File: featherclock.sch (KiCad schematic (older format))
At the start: 49 parts, among them J1 feather long, J2 feather short, J3 Conn_01x04, J4 USB_C_Receptacle_USB2.0, Q1 MMBT3904, Q2 MMBT3904, SW1 SW_Push, U1 ESP8285, U2 DS3231MZ, U3 74AHCT1G125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

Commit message: Updated most 0603 packages to 0402
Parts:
- C1, C2: footprint Capacitor_SMD:C_0603_1608Metric -> Capacitor_SMD:C_0402_1005Metric; LCSC C15849 -> C52923
- C10, C11, C12, C13, C4, C5, C9: footprint Capacitor_SMD:C_0603_1608Metric -> Capacitor_SMD:C_0402_1005Metric; LCSC C14663 -> C1525
- L1: footprint Inductors_SMD:L_0603 -> Inductors_SMD:L_0402; LCSC C1030 -> C13595
- R1, R12, R3, R4, R5, R6, R8, R9: footprint Resistor_SMD:R_0603_1608Metric -> Resistor_SMD:R_0402_1005Metric; LCSC C23162 -> C25900
- R10, R11: footprint Resistor_SMD:R_0603_1608Metric -> Resistor_SMD:R_0402_1005Metric; LCSC C25804 -> C25744
- R13, R14: footprint Resistor_SMD:R_0603_1608Metric -> Resistor_SMD:R_0402_1005Metric; LCSC C23186 -> C25905
- R2: footprint Resistor_SMD:R_0603_1608Metric -> Resistor_SMD:R_0402_1005Metric; LCSC C22790 -> C25752
- R7: footprint Resistor_SMD:R_0603_1608Metric -> Resistor_SMD:R_0402_1005Metric; LCSC C22775 -> C25076
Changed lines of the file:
@@
 F 0 "R2" H 3320 3896 50  0000 L CNN
 F 1 "12K" H 3320 3805 50  0000 L CNN
-F 2 "Resistor_SMD:R_0603_1608Metric" V 3180 3850 50  0001 C CNN
+F 2 "Resistor_SMD:R_0402_1005Metric" V 3180 3850 50  0001 C CNN
 F 3 "~" H 3250 3850 50  0001 C CNN
-F 4 "C22790" H 3250 3850 50  0001 C CNN "LCSC"
+F 4 "C25752" H 3250 3850 50  0001 C CNN "LCSC"
 	1    3250 3850
 	1    0    0    -1
@@
 F 0 "R1" H 4170 3296 50  0000 L CNN
 F 1 "4.7K" H 4170 3205 50  0000 L CNN
-F 2 "Resistor_SMD:R_0603_1608Metric" V 4030 3250 50  0001 C CNN
+F 2 "Resistor_SMD:R_0402_1005Metric" V 4030 3250 50  0001 C CNN
 F 3 "~" H 4100 3250 50  0001 C CNN
-F 4 "C23162" H 4100 3250 50  0001 C CNN "LCSC"
+F 4 "C25900" H 4100 3250 50  0001 C CNN "LCSC"
 	1    4100 3250
 	1    0    0    -1
@@
 F 0 "R4" H 2820 4446 50  0000 L CNN
 F 1 "4.7K" H 2820 4355 50  0000 L CNN
-F 2 "Resistor_SMD:R_0603_1608Metric" V 2680 4400 50  0001 C CNN
+F 2 "Resistor_SMD:R_0402_1005Metric" V 2680 4400 50  0001 C CNN
 F 3 "~" H 2750 4400 50  0001 C CNN
-F 4 "C23162" H 2750 4400 50  0001 C CNN "LCSC"
+F 4 "C25900" H 2750 4400 50  0001 C CNN "LCSC"
 	1    2750 4400
 	1    0    0    -1
@@
 F 0 "C1" H 8265 3846 50  0000 L CNN
 F 1 "1u" H 8265 3755 50  0000 L CNN
-F 2 "Capacitor_SMD:C_0603_1608Metric" H 8188 3650 50  0001 C CNN
+F 2 "Capacitor_SMD:C_0402_1005Metric" H 8188 3650 50  0001 C CNN
 F 3 "~" H 8150 3800 50  0001 C CNN
-F 4 "C15849" H 8150 3800 50  0001 C CNN "LCSC"
+F 4 "C52923" H 8150 3800 50  0001 C CNN "LCSC"
 	1    8150 3800
 	1    0    0    -1
@@
 F 0 "C2" H 8765 3846 50  0000 L CNN
 F 1 "1u" H 8765 3755 50  0000 L CNN
-F 2 "Capacitor_SMD:C_0603_1608Metric" H 8688 3650 50  0001 C CNN
+F 2 "Capacitor_SMD:C_0402_1005Metric" H 8688 3650 50  0001 C CNN
 F 3 "~" H 8650 3800 50  0001 C CNN
-F 4 "C15849" H 8650 3800 50  0001 C CNN "LCSC"
+F 4 "C52923" H 8650 3800 50  0001 C CNN "LCSC"
 	1    8650 3800
 	1    0    0    -1
@@
 F 0 "C4" H 9765 3846 50  0000 L CNN
 F 1 "100n" H 9765 3755 50  0000 L CNN
-F 2 "Capacitor_SMD:C_0603_1608Metric" H 9688 3650 50  0001 C CNN
+F 2 "Capacitor_SMD:C_0402_1005Metric" H 9688 3650 50  0001 C CNN
 F 3 "~" H 9650 3800 50  0001 C CNN
-F 4 "C14663" H 9650 3800 50  0001 C CNN "LCSC"
+F 4 "C1525" H 9650 3800 50  0001 C CNN "LCSC"
 	1    9650 3800
 	1    0    0    -1
@@
 F 0 "R3" H 2570 4446 50  0000 L CNN
 F 1 "4.7K" H 2570 4355 50  0000 L CNN
-F 2 "Resistor_SMD:R_0603_1608Metric" V 2430 4400 50  0001 C CNN
+F 2 "Resistor_SMD:R_0402_1005Metric" V 2430 4400 50  0001 C CNN
 F 3 "~" H 2500 4400 50  0001 C CNN
-F 4 "C23162" H 2500 4400 50  0001 C CNN "LCSC"
+F 4 "C25900" H 2500 4400 50  0001 C CNN "LCSC"
 	1    2500 4400
 	1    0    0    -1
@@
 F 0 "C5" H 6115 3296 50  0000 L CNN
 F 1 "100n" H 6115 3205 50  0000 L CNN
-F 2 "Capacitor_SMD:C_0603_1608Metric" H 6038 3100 50  0001 C CNN
+F 2 "Capacitor_SMD:C_0402_1005Metric" H 6038 3100 50  0001 C CNN
 F 3 "~" H 6000 3250 50  0001 C CNN
-F 4 "C14663" H 6000 3250 50  0001 C CNN "LCSC"
+F 4 "C1525" H 6000 3250 50  0001 C CNN "LCSC"
 	1    6000 3250
 	1    0    0    -1
@@
 F 0 "L1" V 6440 3000 50  0000 C CNN
 F 1 "4.7n" V 6349 3000 50  0000 C CNN
-F 2 "Inductors_SMD:L_0603" H 6250 3000 50  0001 C CNN
+F 2 "Inductors_SMD:L_0402" H 6250 3000 50  0001 C CNN
 F 3 "~" H 6250 3000 50  0001 C CNN
-F 4 "C1030" V 6250 3000 50  0001 C CNN "LCSC"
+F 4 "C13595" V 6250 3000 50  0001 C CNN "LCSC"
 	1    6250 3000
 	0    -1   -1   0
@@
 F 0 "R7" V 5543 6500 50  0000 C CNN
 F 1 "100" V 5634 6500 50  0000 C CNN
-F 2 "Resistor_SMD:R_0603_1608Metric" V 5680 6500 50  0001 C CNN
+F 2 "Resistor_SMD:R_0402_1005Metric" V 5680 6500 50  0001 C CNN
 F 3 "~" H 5750 6500 50  0001 C CNN
-F 4 "C22775" H 5750 6500 50  0001 C CNN "LCSC"
+F 4 "C25076" H 5750 6500 50  0001 C CNN "LCSC"
 	1    5750 6500
 	0    1    1    0
@@
 F 0 "R5" H 2620 2246 50  0000 L CNN
 F 1 "4.7K" H 2620 2155 50  0000 L CNN
-F 2 "Resistor_SMD:R_0603_1608Metric" V 2480 2200 50  0001 C CNN
+F 2 "Resistor_SMD:R_0402_1005Metric" V 2480 2200 50  0001 C CNN
 F 3 "~" H 2550 2200 50  0001 C CNN
-F 4 "C23162" H 2550 2200 50  0001 C CNN "LCSC"
+F 4 "C25900" H 2550 2200 50  0001 C CNN "LCSC"
 	1    2550 2200
 	0    -1   -1   0
@@
 F 0 "R9" H 3570 5296 50  0000 L CNN
 F 1 "4.7K" H 3570 5205 50  0000 L CNN
-F 2 "Resistor_SMD:R_0603_1608Metric" V 3430 5250 50  0001 C CNN
+F 2 "Resistor_SMD:R_0402_1005Metric" V 3430 5250 50  0001 C CNN
 F 3 "~" H 3500 5250 50  0001 C CNN
-F 4 "C23162" H 3500 5250 50  0001 C CNN "LCSC"
+F 4 "C25900" H 3500 5250 50  0001 C CNN "LCSC"
 	1    3500 5250
 	-1   0    0    1
@@
 F 0 "C11" H 5615 6196 50  0000 L CNN
 F 1 "100n" H 5615 6105 50  0000 L CNN
-F 2 "Capacitor_SMD:C_0603_1608Metric" H 5538 6000 50  0001 C CNN
+F 2 "Capacitor_SMD:C_0402_1005Metric" H 5538 6000 50  0001 C CNN
 F 3 "~" H 5500 6150 50  0001 C CNN
-F 4 "C14663" H 5500 6150 50  0001 C CNN "LCSC"
+F 4 "C1525" H 5500 6150 50  0001 C CNN "LCSC"
 	1    5500 6150
 	1    0    0    -1
@@
 F 0 "R11" V 1293 7300 50  0000 C CNN
 F 1 "10K" V 1384 7300 50  0000 C CNN
-F 2 "Resistor_SMD:R_0603_1608Metric" V 1430 7300 50  0001 C CNN
+F 2 "Resistor_SMD:R_0402_1005Metric" V 1430 7300 50  0001 C CNN
 F 3 "~" H 1500 7300 50  0001 C CNN
-F 4 "C25804" H 1500 7300 50  0001 C CNN "LCSC"
+F 4 "C25744" H 1500 7300 50  0001 C CNN "LCSC"
 	1    1500 7300
 	0    1    1    0
@@
 F 0 "R10" V 1293 6700 50  0000 C CNN
 F 1 "10K" V 1384 6700 50  0000 C CNN
-F 2 "Resistor_SMD:R_0603_1608Metric" V 1430 6700 50  0001 C CNN
+F 2 "Resistor_SMD:R_0402_1005Metric" V 1430 6700 50  0001 C CNN
 F 3 "~" H 1500 6700 50  0001 C CNN
-F 4 "C25804" H 1500 6700 50  0001 C CNN "LCSC"
+F 4 "C25744" H 1500 6700 50  0001 C CNN "LCSC"
 	1    1500 6700
 	0    1    1    0
@@
 F 0 "R6" H 3870 3296 50  0000 L CNN
 F 1 "4.7K" H 3870 3205 50  0000 L CNN
-F 2 "Resistor_SMD:R_0603_1608Metric" V 3730 3250 50  0001 C CNN
+F 2 "Resistor_SMD:R_0402_1005Metric" V 3730 3250 50  0001 C CNN
 F 3 "~" H 3800 3250 50  0001 C CNN
-F 4 "C23162" H 3800 3250 50  0001 C CNN "LCSC"
+F 4 "C25900" H 3800 3250 50  0001 C CNN "LCSC"
 	1    3800 3250
 	1    0    0    -1
@@
 F 0 "R12" H 3920 9246 50  0000 L CNN
 F 1 "4.7K" H 3920 9155 50  0000 L CNN
-F 2 "Resistor_SMD:R_0603_1608Metric" V 3780 9200 50  0001 C CNN
+F 2 "Resistor_SMD:R_0402_1005Metric" V 3780 9200 50  0001 C CNN
 F 3 "~" H 3850 9200 50  0001 C CNN
-F 4 "C23162" H 3850 9200 50  0001 C CNN "LCSC"
+F 4 "C25900" H 3850 9200 50  0001 C CNN "LCSC"
 	1    3850 9200
 	0    -1   -1   0
@@
 F 0 "C13" H 4465 9546 50  0000 L CNN
 F 1 "100n" H 4465 9455 50  0000 L CNN
-F 2 "Capacitor_SMD:C_0603_1608Metric" H 4388 9350 50  0001 C CNN
+F 2 "Capacitor_SMD:C_0402_1005Metric" H 4388 9350 50  0001 C CNN
 F 3 "~" H 4350 9500 50  0001 C CNN
-F 4 "C14663" H 4350 9500 50  0001 C CNN "LCSC"
+F 4 "C1525" H 4350 9500 50  0001 C CNN "LCSC"
 	1    4350 9500
 	1    0    0    -1
@@
 F 0 "C12" H 2665 9196 50  0000 L CNN
 F 1 "100n" H 2665 9105 50  0000 L CNN
-F 2 "Capacitor_SMD:C_0603_1608Metric" H 2588 9000 50  0001 C CNN
+F 2 "Capacitor_SMD:C_0402_1005Metric" H 2588 9000 50  0001 C CNN
 F 3 "~" H 2550 9150 50  0001 C CNN
-F 4 "C14663" H 2550 9150 50  0001 C CNN "LCSC"
+F 4 "C1525" H 2550 9150 50  0001 C CNN "LCSC"
 	1    2550 9150
 	1    0    0    -1
@@
 F 0 "R14" V 2193 10050 50  0000 C CNN
 F 1 "5.1K" V 2284 10050 50  0000 C CNN
-F 2 "Resistor_SMD:R_0603_1608Metric" V 2330 10050 50  0001 C CNN
+F 2 "Resistor_SMD:R_0402_1005Metric" V 2330 10050 50  0001 C CNN
 F 3 "~" H 2400 10050 50  0001 C CNN
-F 4 "C23186" H 2400 10050 50  0001 C CNN "LCSC"
+F 4 "C25905" H 2400 10050 50  0001 C CNN "LCSC"
 	1    2400 10050
 	-1   0    0    1
@@
 F 0 "R13" V 1993 10050 50  0000 C CNN
 F 1 "5.1K" V 2084 10050 50  0000 C CNN
-F 2 "Resistor_SMD:R_0603_1608Metric" V 2130 10050 50  0001 C CNN
+F 2 "Resistor_SMD:R_0402_1005Metric" V 2130 10050 50  0001 C CNN
 F 3 "~" H 2200 10050 50  0001 C CNN
-F 4 "C23186" H 2200 10050 50  0001 C CNN "LCSC"
+F 4 "C25905" H 2200 10050 50  0001 C CNN "LCSC"
 	1    2200 10050
 	-1   0    0    1
@@
 F 0 "R8" H 2320 4446 50  0000 L CNN
 F 1 "4.7K" H 2320 4355 50  0000 L CNN
-F 2 "Resistor_SMD:R_0603_1608Metric" V 2180 4400 50  0001 C CNN
+F 2 "Resistor_SMD:R_0402_1005Metric" V 2180 4400 50  0001 C CNN
 F 3 "~" H 2250 4400 50  0001 C CNN
-F 4 "C23162" H 2250 4400 50  0001 C CNN "LCSC"
+F 4 "C25900" H 2250 4400 50  0001 C CNN "LCSC"
 	1    2250 4400
 	1    0    0    -1
@@
 F 0 "C10" H 7865 1546 50  0000 L CNN
 F 1 "100n" H 7865 1455 50  0000 L CNN
-F 2 "Capacitor_SMD:C_0603_1608Metric" H 7788 1350 50  0001 C CNN
+F 2 "Capacitor_SMD:C_0402_1005Metric" H 7788 1350 50  0001 C CNN
 F 3 "~" H 7750 1500 50  0001 C CNN
-F 4 "C14663" H 7750 1500 50  0001 C CNN "LCSC"
+F 4 "C1525" H 7750 1500 50  0001 C CNN "LCSC"
 	1    7750 1500
 	1    0    0    -1
@@
 F 0 "C9" H 5215 1546 50  0000 L CNN
 F 1 "100n" H 5215 1455 50  0000 L CNN
-F 2 "Capacitor_SMD:C_0603_1608Metric" H 5138 1350 50  0001 C CNN
+F 2 "Capacitor_SMD:C_0402_1005Metric" H 5138 1350 50  0001 C CNN
 F 3 "~" H 5100 1500 50  0001 C CNN
-F 4 "C14663" H 5100 1500 50  0001 C CNN "LCSC"
+F 4 "C1525" H 5100 1500 50  0001 C CNN "LCSC"
 	1    5100 1500
 	1    0    0    -1

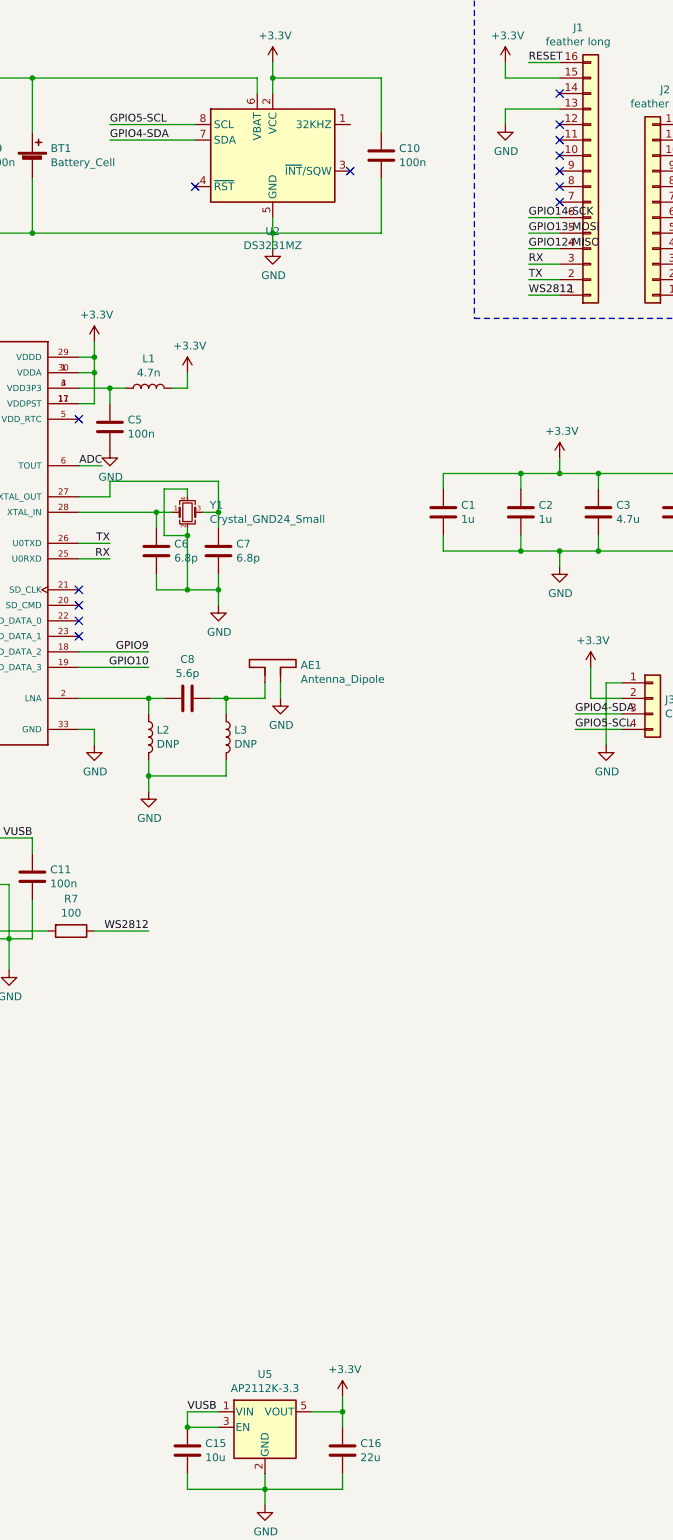
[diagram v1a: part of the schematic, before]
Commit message: Adding ADC and enable pins
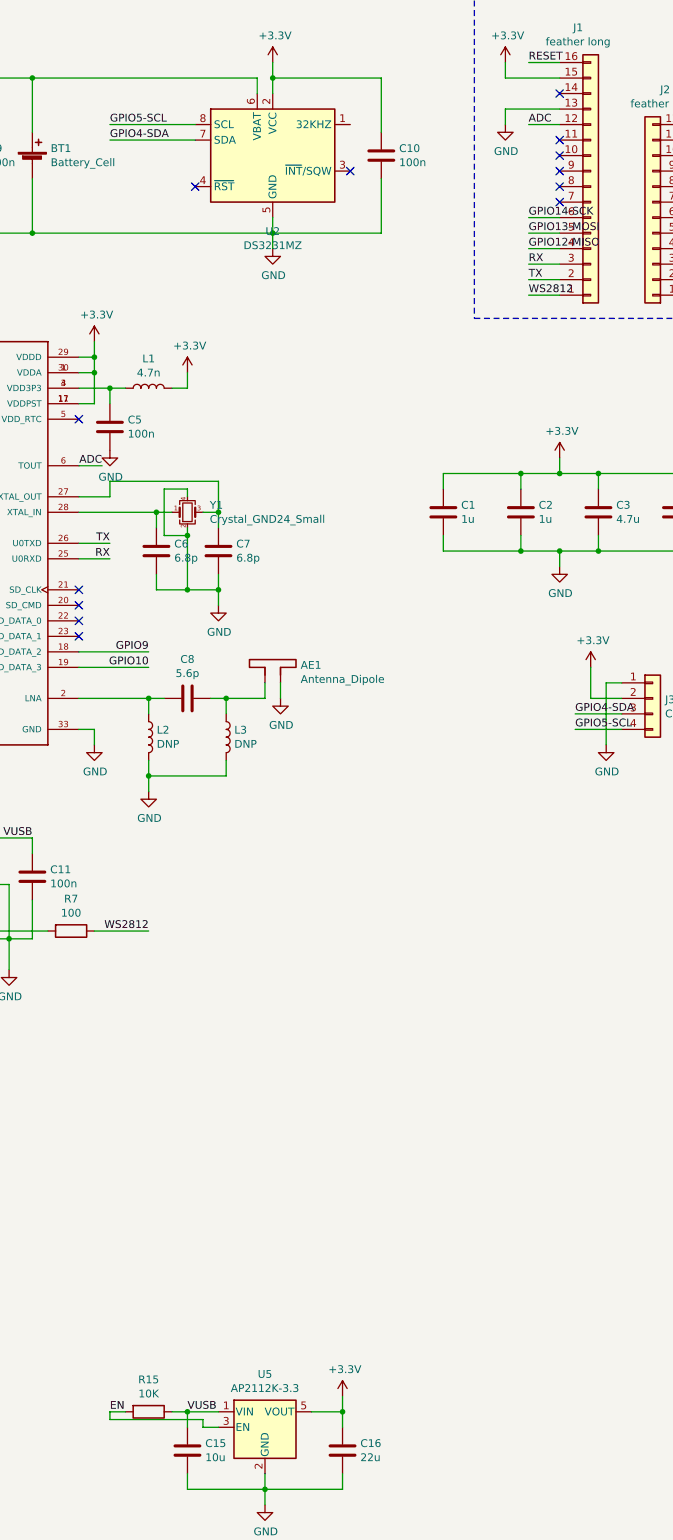
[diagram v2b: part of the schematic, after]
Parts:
- added R15: 10K, Resistor_SMD:R_0402_1005Metric, symbol Device:R
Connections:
- net ADC: now also J1.12 (Pin_12)
- net EN: now also U5.3 (EN), R15.2
- net VCC: now also R15.1; no longer U5.3 (EN)
- no-connect marks 22 -> 21
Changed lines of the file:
@@
 	6500 10100 6500 10000
-Wire Wire Line
-	6700 9700 6500 9700
 Wire Wire Line
 	6700 9600 6500 9600
 Wire Wire Line
 	6500 9600 6500 9700
-Connection ~ 6500 9700
 Text Label 6500 9600 0    50   ~ 0
 VUSB
@@
 	7500 9500 7500 9600
 Connection ~ 7500 9600
-NoConn ~ 8900 1300
+Wire Wire Line
+	8900 1300 8700 1300
+Text Label 8700 1300 0    50   ~ 0
+ADC
+$Comp
+L Device:R R15
+U 1 1 612DBEC5
+P 6250 9600
+F 0 "R15" V 6043 9600 50  0000 C CNN
+F 1 "10K" V 6134 9600 50  0000 C CNN
+F 2 "Resistor_SMD:R_0402_1005Metric" V 6180 9600 50  0001 C CNN
+F 3 "~" H 6250 9600 50  0001 C CNN
+F 4 "C25744" H 6250 9600 50  0001 C CNN "LCSC"
+	1    6250 9600
+	0    1    1    0
+$EndComp
+Wire Wire Line
+	6400 9600 6500 9600
+Connection ~ 6500 9600
+Wire Wire Line
+	6700 9700 6600 9700
+Wire Wire Line
+	6600 9700 6600 9650
+Wire Wire Line
+	6600 9650 6000 9650
+Wire Wire Line
+	6000 9650 6000 9600
+Wire Wire Line
+	6000 9600 6100 9600
+Text Label 6000 9600 0    50   ~ 0
+EN
 $EndSCHEMATC
